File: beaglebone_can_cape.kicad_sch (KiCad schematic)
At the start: 20 parts, among them J1 DCAN0, J2 DCAN1, P8 BeagleBone_Black_Header, P9 BeagleBone_Black_Header, U1 TCAN332, U2 TCAN332, U3 LMR51430

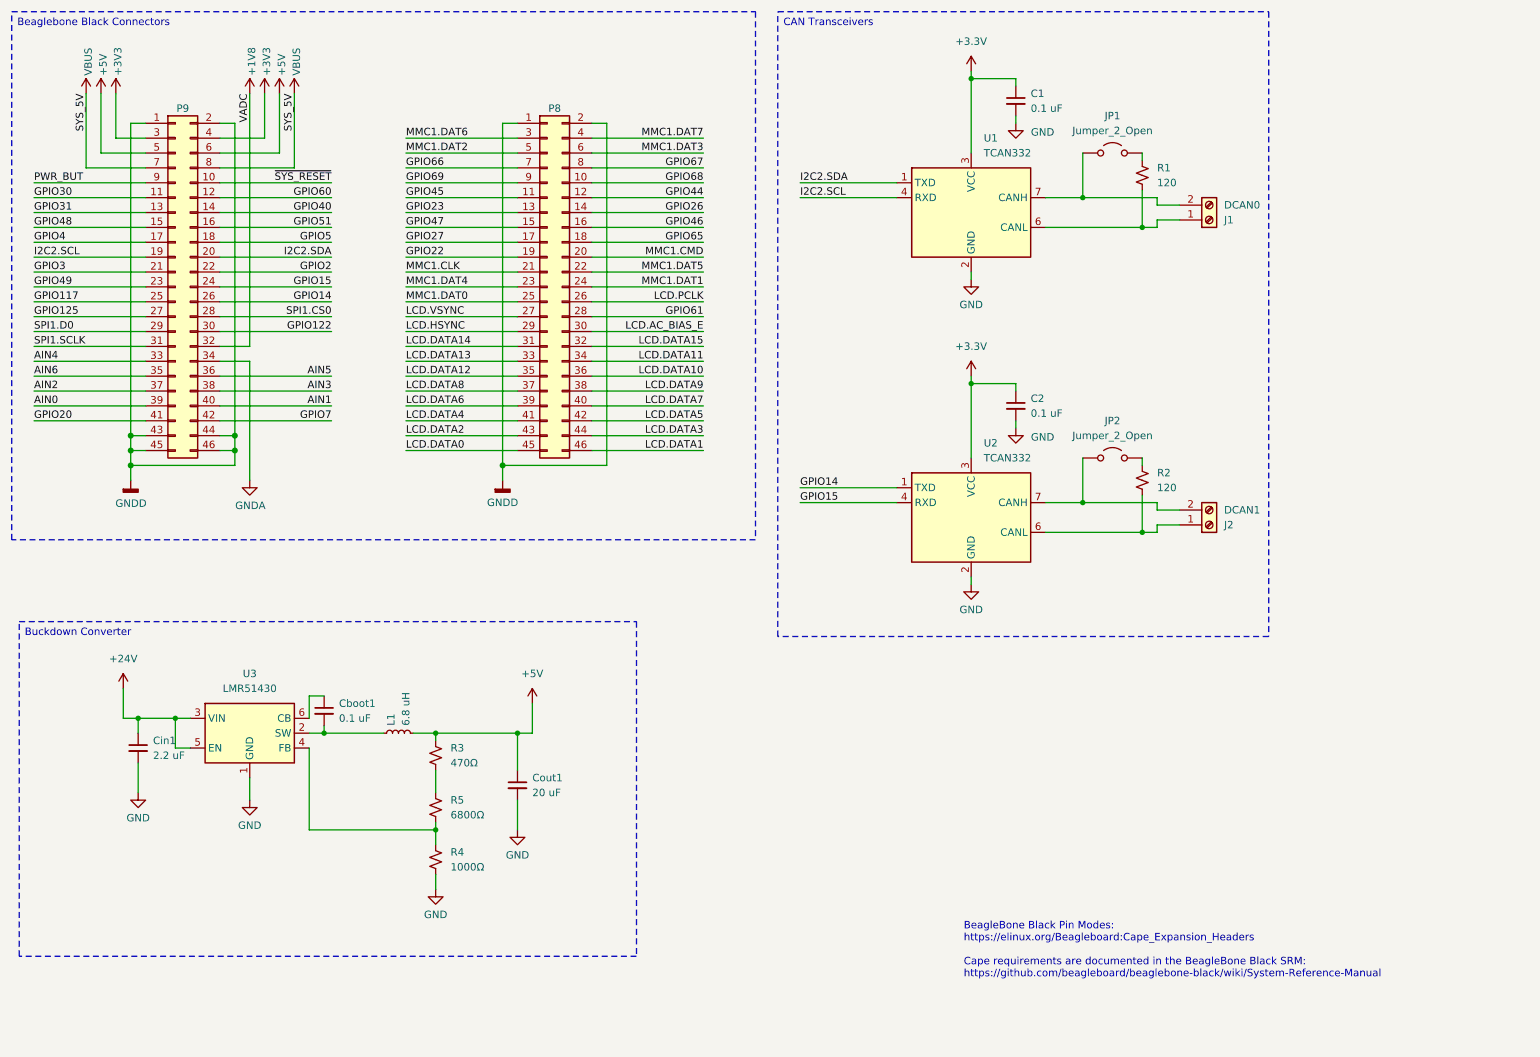
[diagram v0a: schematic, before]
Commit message: Finished with schematic
Did research on TCAN332 vs SN65HVD230, trying TCAN332 first. All footprints loaded.
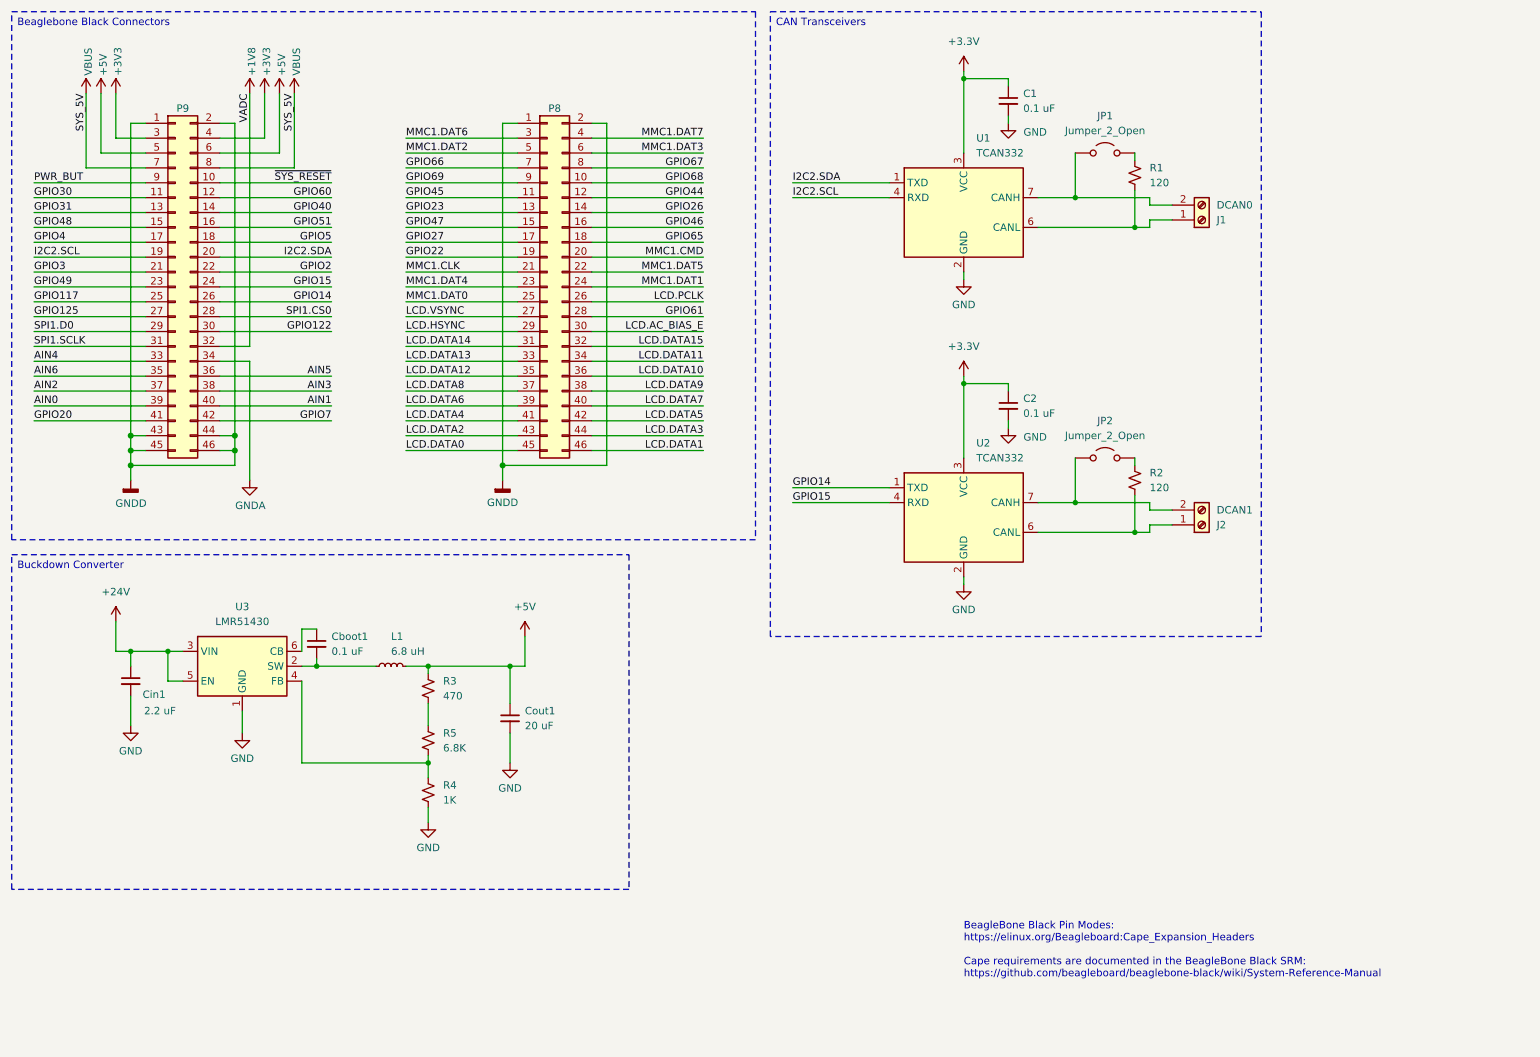
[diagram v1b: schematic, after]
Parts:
- C1, C2: footprint (none) -> Capacitor_SMD:C_0805_2012Metric
- Cboot1, Cin1, Cout1: footprint Capacitor_THT:CP_Axial_L10.0mm_D4.5mm_P15.00mm_Horizontal -> Capacitor_SMD:C_0805_2012Metric
- R1, R2: footprint Resistor_THT:R_Axial_DIN0204_L3.6mm_D1.6mm_P1.90mm_Vertical -> Resistor_SMD:R_0805_2012Metric
- R3: value 470Ω -> 470; footprint Resistor_THT:R_Axial_DIN0204_L3.6mm_D1.6mm_P1.90mm_Vertical -> Resistor_SMD:R_0805_2012Metric
- R4: value 1000Ω -> 1K; footprint Resistor_THT:R_Axial_DIN0204_L3.6mm_D1.6mm_P1.90mm_Vertical -> Resistor_SMD:R_0805_2012Metric
- R5: value 6800Ω -> 6.8K; footprint Resistor_THT:R_Axial_DIN0204_L3.6mm_D1.6mm_P1.90mm_Vertical -> Resistor_SMD:R_0805_2012Metric
- U1, U2: footprint (none) -> Senior Design:D0008A_M
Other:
- moved on the sheet: C1, C2, Cboot1, Cin1, Cout1, J1, J2, JP1, JP2, L1, R1, R2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

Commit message: Laid out CAN on PCB
'Nuff said
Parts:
- L1: footprint Inductor_THT:L_Axial_L5.0mm_D3.6mm_P10.00mm_Horizontal_Murata_BL01RN1A2A2 -> Inductor_SMD:L_0805_2012Metric
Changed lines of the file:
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@@
 			)
 		)
-		(property "Footprint" "Inductor_THT:L_Axial_L5.0mm_D3.6mm_P10.00mm_Horizontal_Murata_BL01RN1A2A2"
+		(property "Footprint" "Inductor_SMD:L_0805_2012Metric"
 			(at 80.01 127 0)
 			(effects

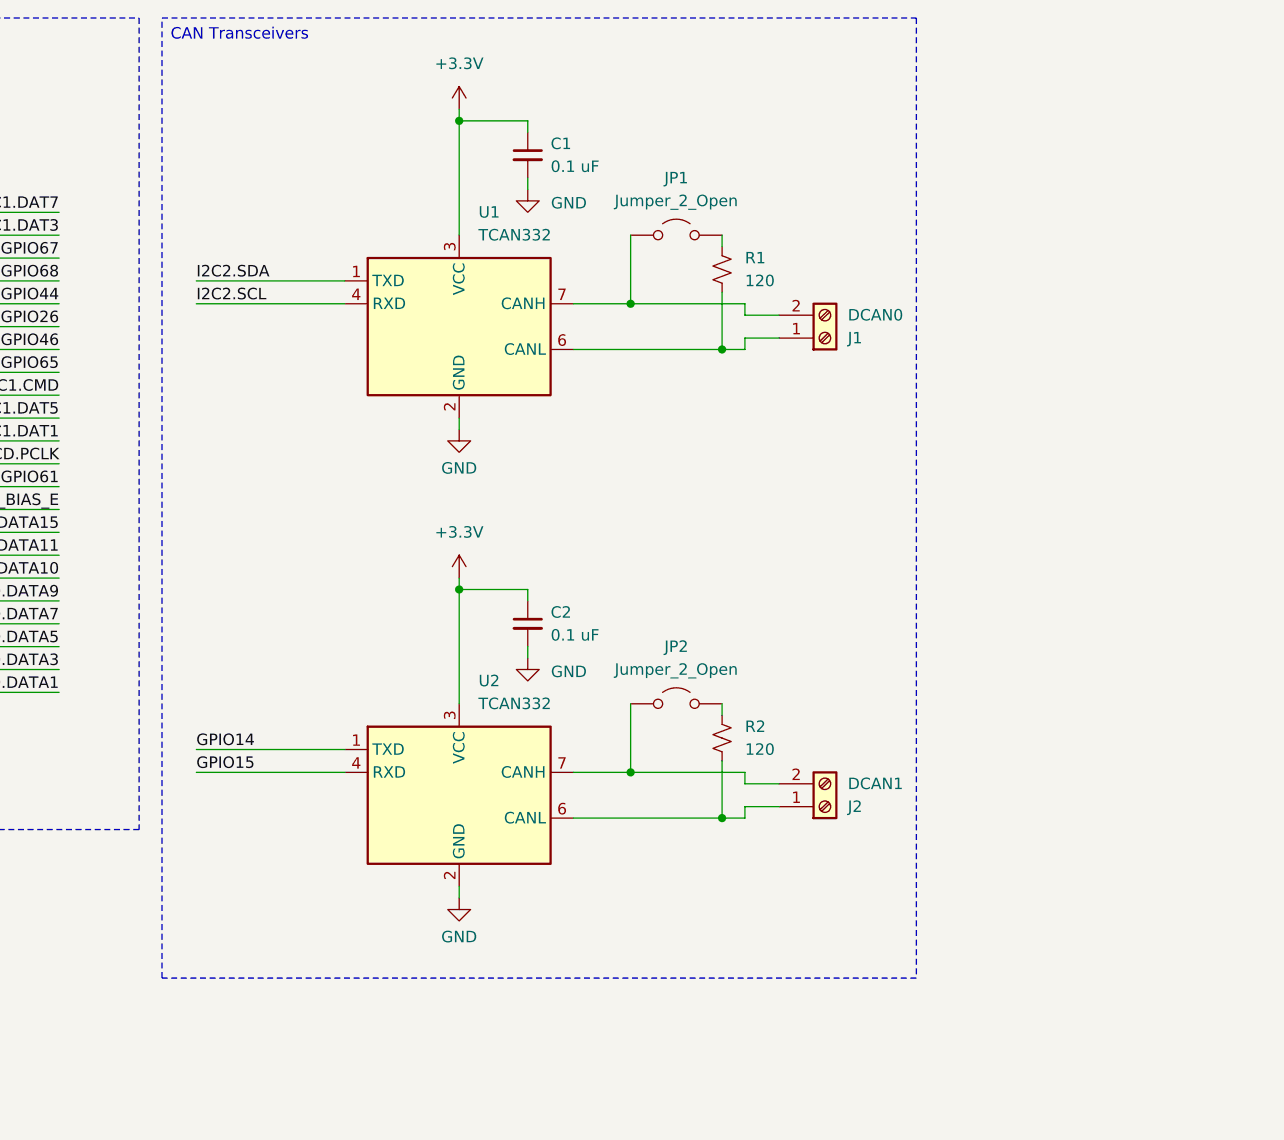
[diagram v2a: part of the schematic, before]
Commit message: PCB and SCH updates
Just moved some text boxes, footprints, and explored ideas for the Deutsch connectors.

Co-Authored-By: Zach Weidner <119375087+weidnerz@users.noreply.github.com>
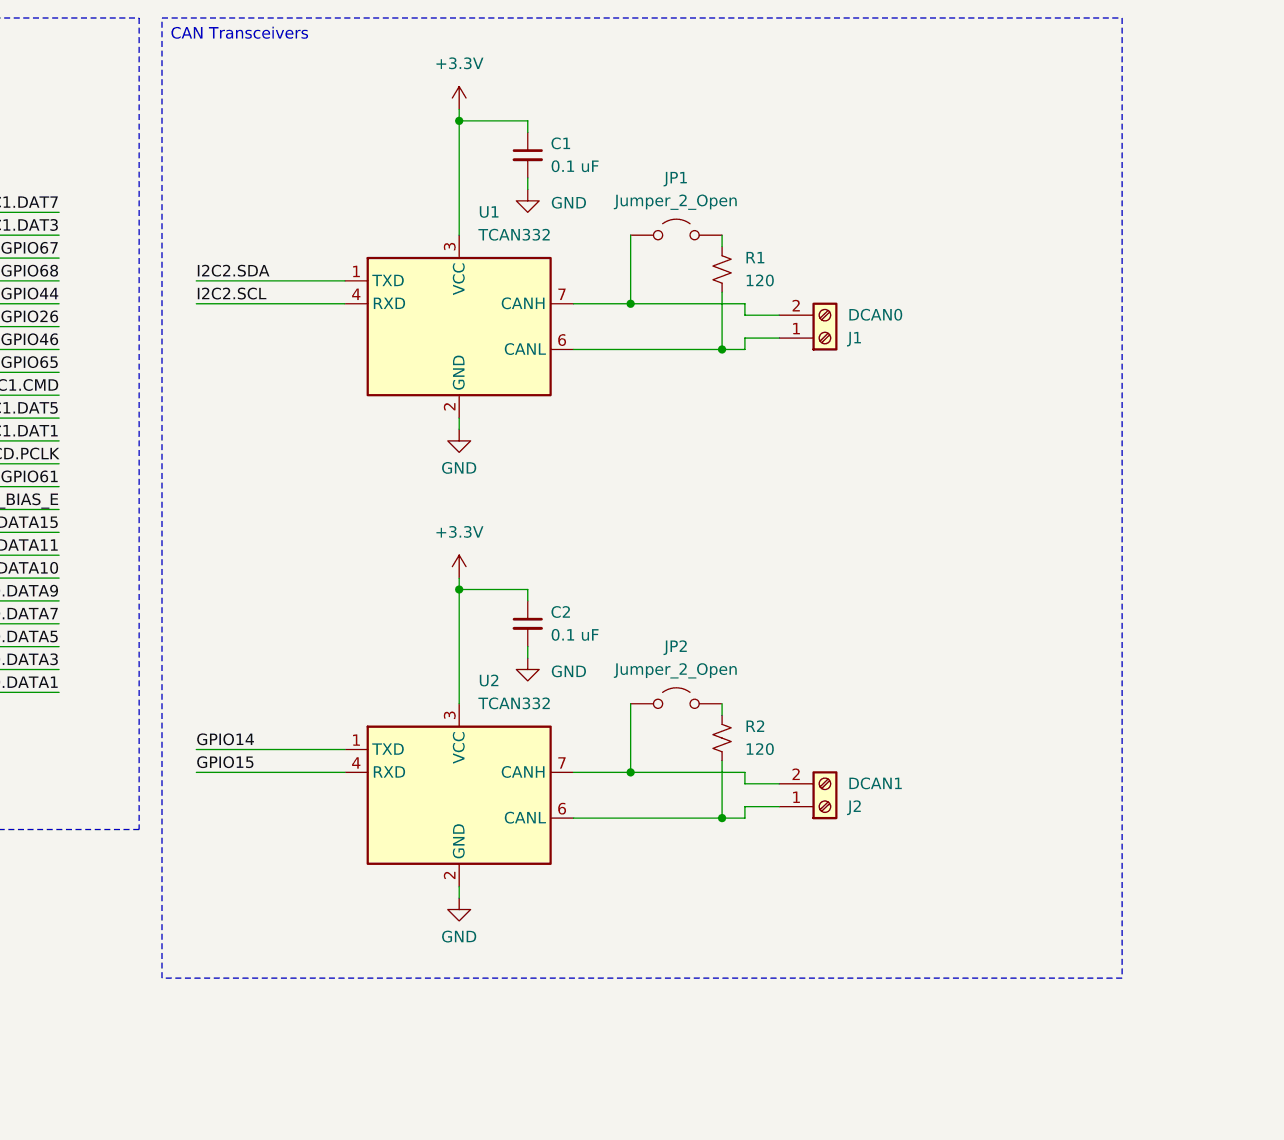
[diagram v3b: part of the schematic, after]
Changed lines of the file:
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@@
 		(exclude_from_sim no)
 		(at 144.78 15.24 0)
-		(size 83.82 106.68)
+		(size 106.68 106.68)
 		(margins 0.9525 0.9525 0.9525 0.9525)
 		(stroke
